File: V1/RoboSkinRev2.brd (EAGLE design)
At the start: 34.3 x 12.7 mm, 51 parts, among them U1 AK9750, U2 FDC2114RGHT, U3 ADS1015, U4 LSM6DS3DOT_INDICATION, U5 VL53L1XSMD

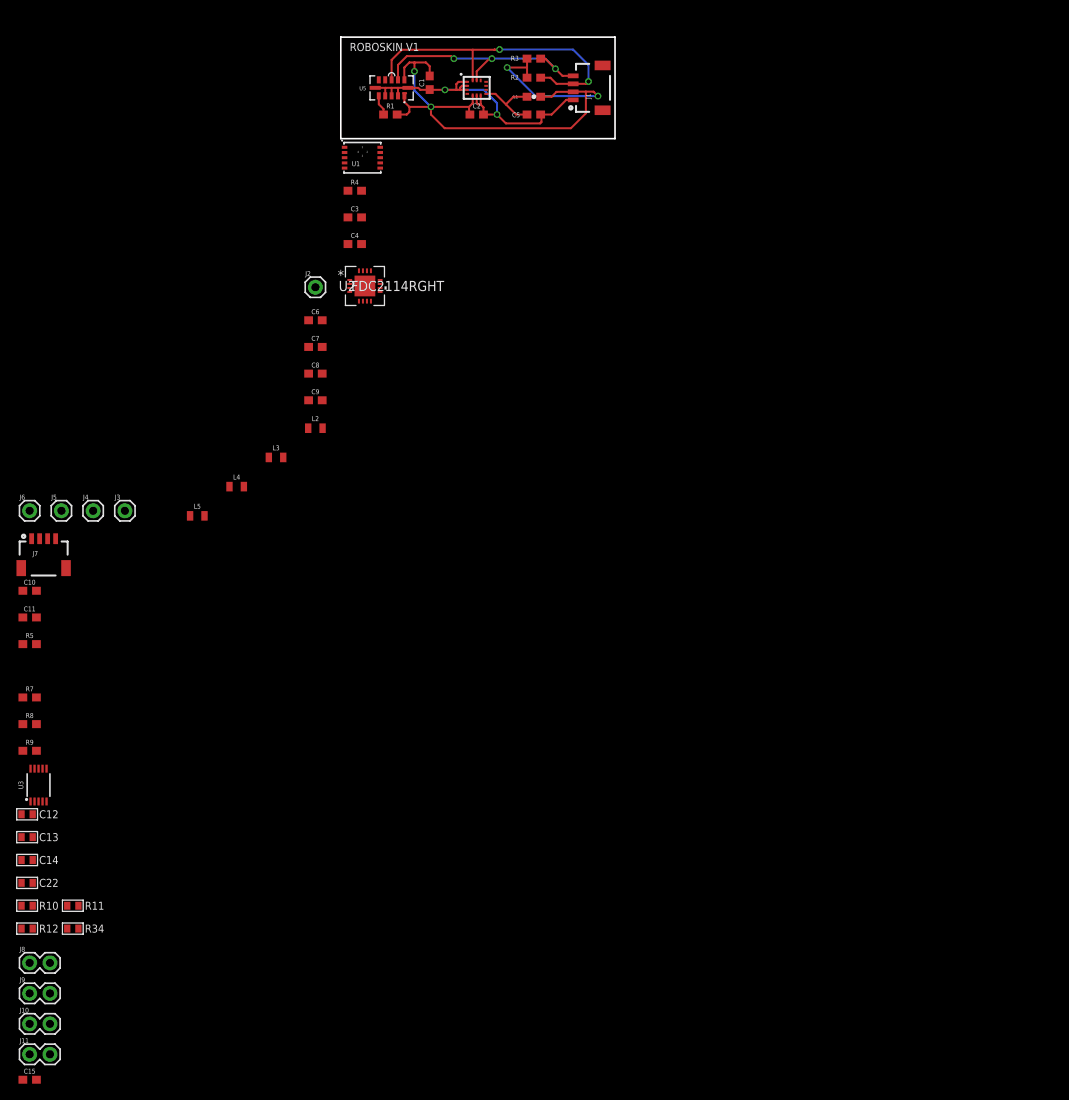
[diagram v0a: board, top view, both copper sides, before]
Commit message: NEw PCB formfactor with added circuits, adding BOM, adding PVF
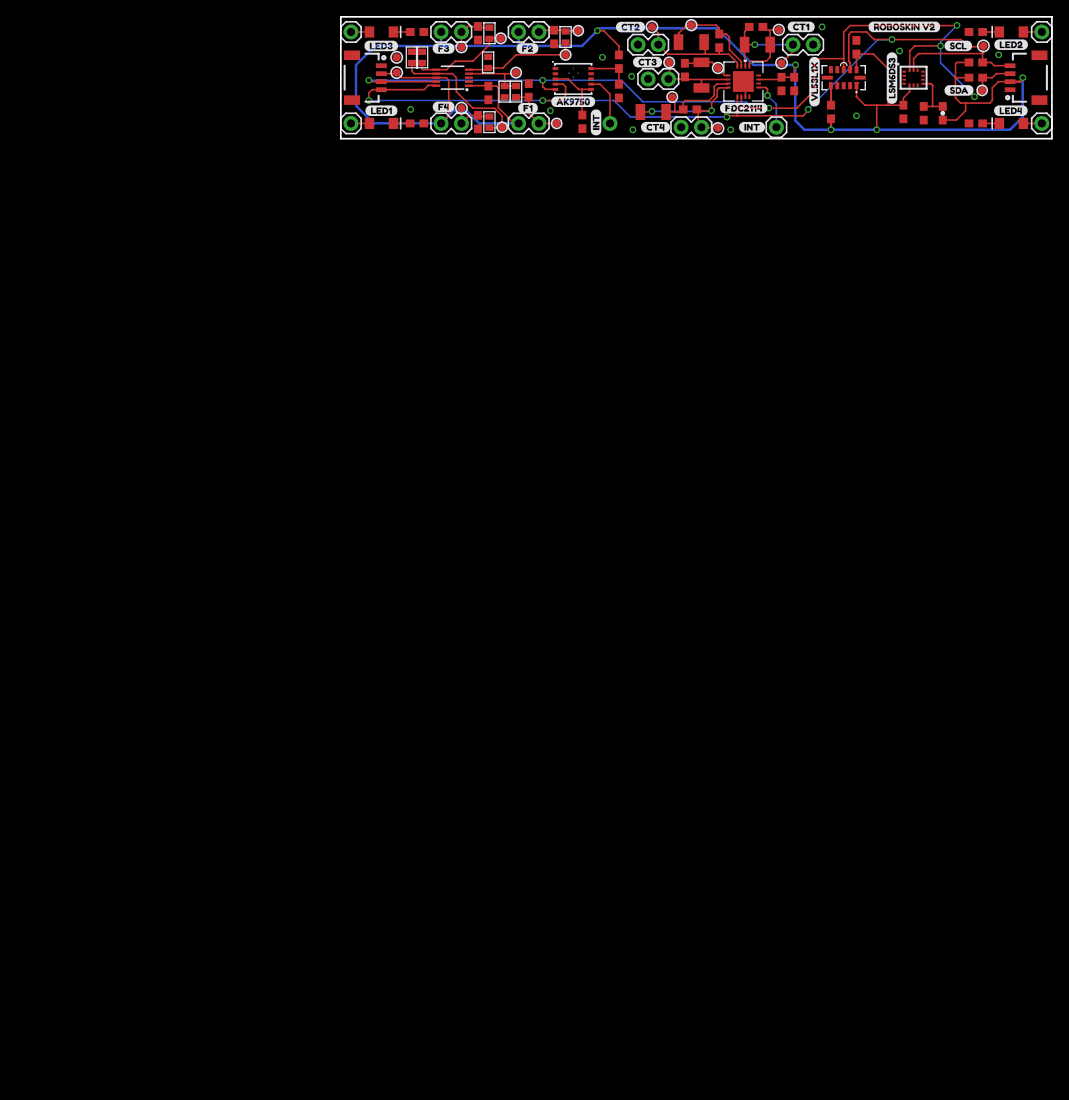
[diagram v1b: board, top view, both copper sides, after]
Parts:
- added D1, D2, D3, D4: (no value), SparkFun-LED:LED-1206
- added J12, J13, J14, J15: (no value), SparkFun-Connectors:1X01
- added J16: (no value), SparkFun-Connectors:1X01_NO_SILK
- added R13, R14, R15, R6: 330, SparkFun-Resistors:0603
- added TP1, TP10, TP11, TP12, TP16, TP17, TP18, TP19, TP2, TP20, TP21, TP22, TP23, TP24, TP3, TP5, TP6, TP7, TP8, TP9: TEST-POINT3X4, SparkFun-Connectors:PAD.03X.04
- added U$24: (no value), buzzard_labels (12):AK975035
- added U$25: (no value), buzzard_labels (12):CT12
- added U$26: (no value), buzzard_labels (12):CT23
- added U$27: (no value), buzzard_labels (12):CT34
- added U$28: (no value), buzzard_labels (12):CT45
- added U$29: (no value), buzzard_labels (12):F16
- added U$30: (no value), buzzard_labels (12):F27
- added U$31: (no value), buzzard_labels (12):F38
- added U$32: (no value), buzzard_labels (12):F49
- added U$34: (no value), buzzard_labels (12):FDC211438
- added U$36, U$46: (no value), buzzard_labels (12):INT30
- added U$37: (no value), buzzard_labels (12):LED131
- added U$38: (no value), buzzard_labels (12):LED232
- added U$39: (no value), buzzard_labels (12):LED333
- added U$40: (no value), buzzard_labels (12):LED434
- added U$41: (no value), buzzard_labels (12):LSM6DS336
- added U$42: (no value), buzzard_labels (12):ROBOSKIN_V241
- added U$43: (no value), buzzard_labels (12):SCL39
- added U$44: (no value), buzzard_labels (12):SDA40
- added U$45: (no value), buzzard_labels (12):VL53L1X37
- J3, J4, J5, J6: device SparkFun-Connectors:1X01 -> SparkFun-Connectors:1X02
- L2, L3, L4, L5: value 10μH_SHIELDED_INDUCTOR0805 -> 18uH; device SparkFun-Coils:0805 -> SparkFun-Retired:1210
- moved C15 136.0 mm to (18.4, 5.71), turned to 270 degrees
- moved J8 132.6 mm to (24.8, 13.3), turned to 180 degrees
- moved J9 131.7 mm to (15.1, 13.3), turned to 180 degrees
- moved J10 129.3 mm to (24.8, 1.91), turned to 180 degrees
- moved J11 128.3 mm to (15.1, 1.91), turned to 180 degrees
- moved R10 127.8 mm to (28.1, 12.7), turned to 90 degrees
- moved R12 121.2 mm to (21.9, 5.87), turned to 270 degrees
- moved R11 120.9 mm to (18.6, 13.2), turned to 90 degrees
- moved C11 116.5 mm to (56.7, 6.83), turned to 270 degrees
- moved C22 113.8 mm to (8.89, 10.2), turned to 90 degrees
- moved R34 113.5 mm to (18.6, 2.06), turned to 90 degrees
- moved C10 113.3 mm to (55.1, 6.83), turned to 270 degrees
- moved C14 113.1 mm to (20.5, 5.87), turned to 270 degrees
- moved J6 111.8 mm to (56.5, 11.7)
- moved R9 110.7 mm to (26.7, 12.7), turned to 270 degrees
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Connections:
- new net D1: D2.A, J13.1
- new net D2: D3.A, J14.1
- new net D3: D4.A, J15.1
- new net D7: D1.A, J12.1
- new net N$11: J16.1, U1.4
- new net N$4: D1.C, R15.2
- new net N$5: D2.C, R6.2
- new net N$7: D3.C, R13.2
- new net N$9: D4.C, R14.2
- net 0: now also TP20.P$1
- net 1: now also TP21.P$1
- net 2: now also TP22.P$1
- net 3: now also TP23.P$1
- net 3.3V: now also TP3.P$1
- net A0: now also TP16.P$1
- net A1: now also TP17.P$1
- net A2: now also TP18.P$1
- net A3: now also TP19.P$1
- net GND: now also J3.2, J4.2, J5.2, J6.2, R13.1, R14.1, R15.1, R6.1, TP24.P$1
- net N$10: now also TP9.P$1
- net N$12: now also TP7.P$1
- net N$14: now also TP5.P$1
- net N$8: now also TP11.P$1
- net PAD1: now also J6.1, TP6.P$1; no longer J3.1
- net PAD2: now also J5.1, TP8.P$1; no longer J4.1
- net PAD3: now also J4.1, TP10.P$1; no longer J5.1
- net PAD4: now also J3.1, TP12.P$1; no longer J6.1
- net SCL: now also TP2.P$1
- net SDA: now also TP1.P$1
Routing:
- net 3.3V: track 76.7 -> 215.9 mm, vias 4 -> 5
- net SCL: track 31.4 -> 126.3 mm, vias 3 -> 5
- net SDA: track 40.8 -> 124.8 mm, vias 2 -> 6
- net GND: track 44.4 -> 3.27 mm, vias 2 -> 10
- net PAD4: track 0.00 -> 20.0 mm, vias 0 -> 2
- net A3: track 0.00 -> 18.7 mm
- net PAD2: track 0.00 -> 16.3 mm
- net A1: track 0.00 -> 14.4 mm
- net PAD1: track 0.00 -> 14.3 mm, vias 0 -> 1
- net N$12: track 0.00 -> 13.2 mm
- net A2: track 0.00 -> 12.7 mm
- net N$8: track 0.00 -> 12.4 mm
- net PAD3: track 0.00 -> 10.9 mm
- net A0: track 0.00 -> 8.92 mm
- net N$14: track 0.00 -> 8.91 mm
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- added copper zone on layer 1, net GND
- added copper zone on layer 16, net GND
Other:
- board size 34.3 x 12.7 mm -> 88.9 x 15.2 mm
- board text removed: "LSM6DS3"
- board text removed: "ROBOSKIN V1"
